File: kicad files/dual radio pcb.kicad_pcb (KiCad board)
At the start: 4 copper layers, 37.7 x 37.7 mm, 65 parts, among them J1 Conn_Coaxial, J2 Conn_01x01_Female, J3 Conn_01x01_Female, J4 Conn_01x01_Female, J5 Conn_01x01_Female, J6 Conn_01x01_Female, J7 Conn_01x04_Male, J8 Conn_Coaxial, J9 Conn_01x01_Female, U1 3V3. 500mA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

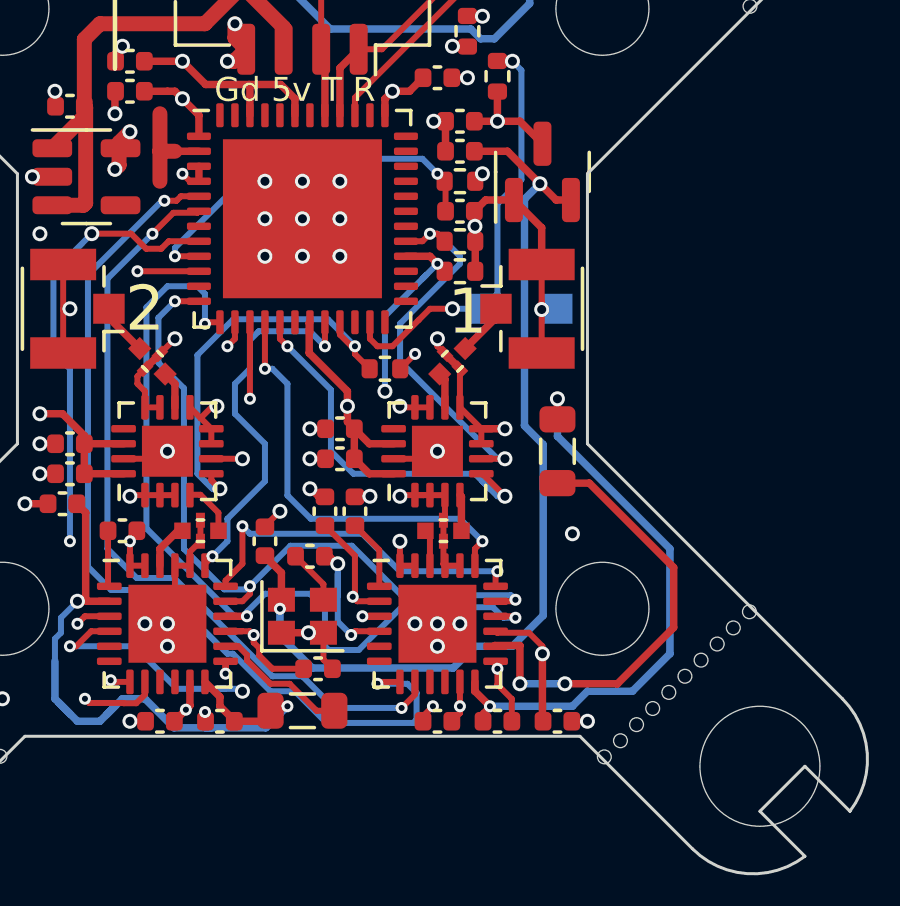
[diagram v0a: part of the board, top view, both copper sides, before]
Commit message: Updated dual radio to eliminate second rad's inductor
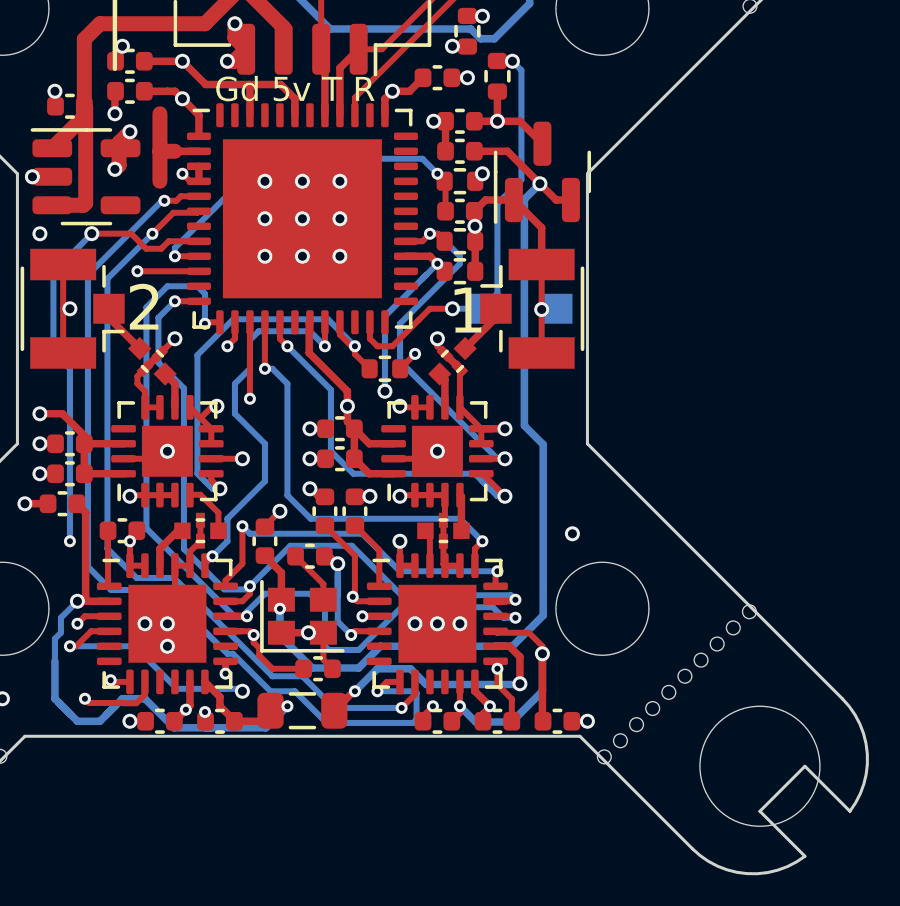
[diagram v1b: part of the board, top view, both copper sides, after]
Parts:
- removed L2: 15u, Inductor_SMD:L_0805_2012Metric
- moved L1 12.1 mm to (142.5, 120.9), turned to 0 degrees
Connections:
- C12 pad 1: /V_DCC_2 -> /V_DCC
- C13 pad 2: /V_DCC_2 -> /V_DCC
- U3 pad 12: /V_DCC_2 -> /V_DCC
- U3 pad 14: /V_DCC2_2 -> unconnected-(U3-Pad14)
- U3 pad 2: /V_DCC_2 -> /V_DCC
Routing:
- net /V_DCC_2: track 21.3 -> 0.00 mm, vias 2 -> 0
- net /V_DCC: track 29.2 -> 40.4 mm, vias 3 -> 4
- net /V_DCC2: track 15.1 -> 8.85 mm
- net +3V3: track 43.6 -> 48.2 mm
- net /V_DCC2_2: track 4.62 -> 0.00 mm
- net GND: vias 60 -> 59

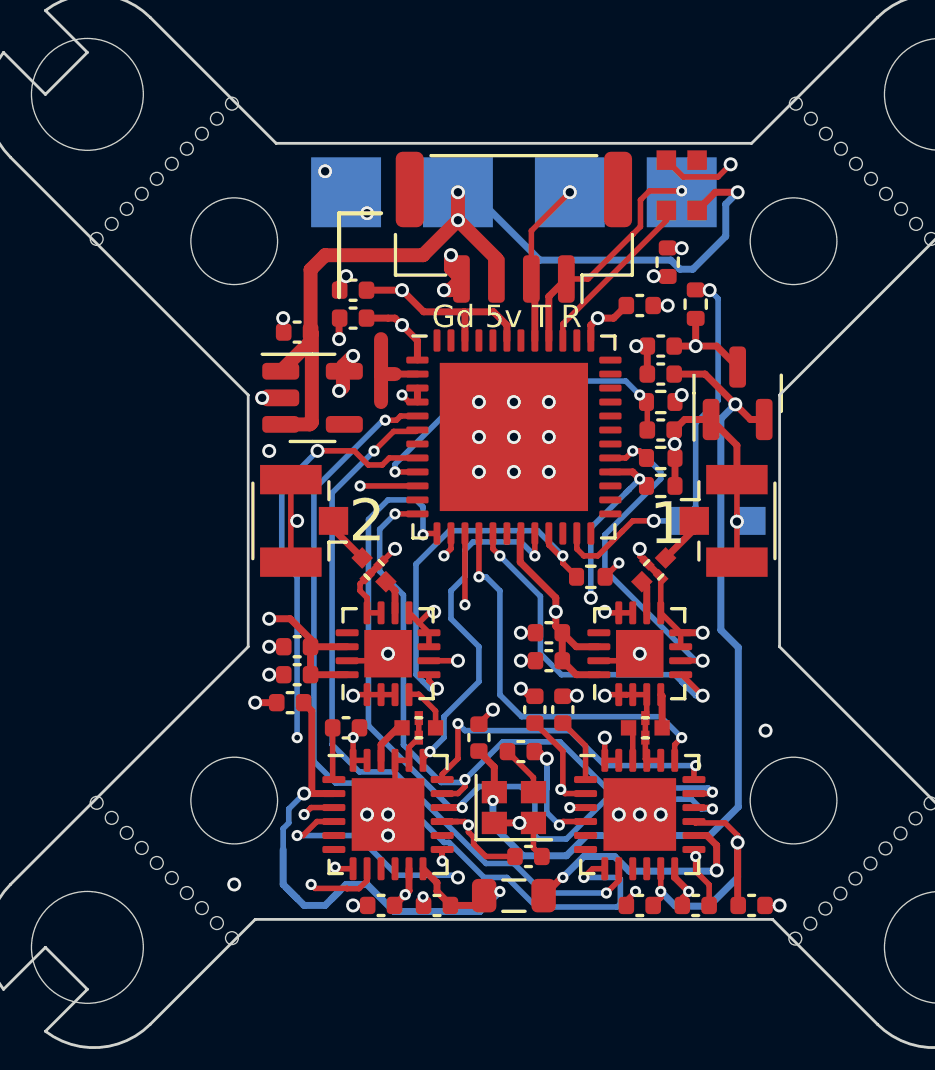
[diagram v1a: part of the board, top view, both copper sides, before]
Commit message: Updates including dif filter by antenna, better WiFi PCB antenna, and single inductor
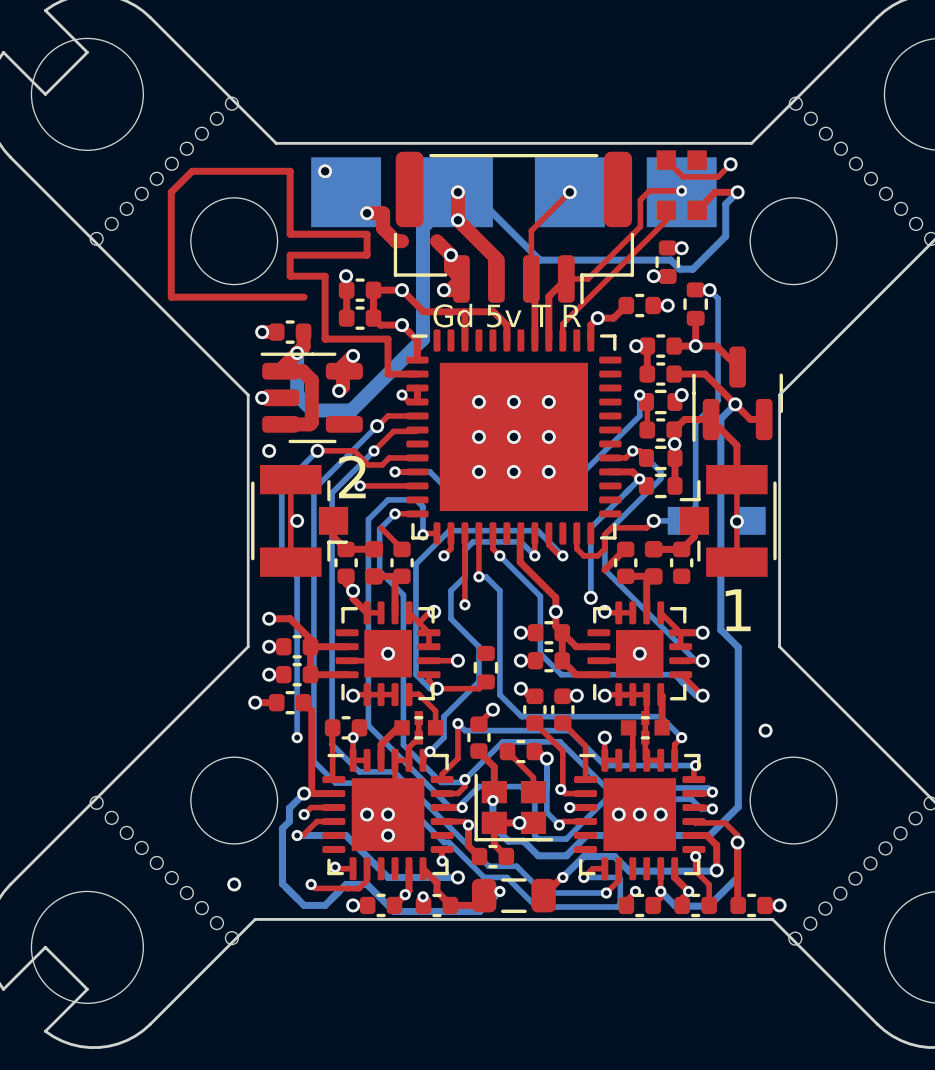
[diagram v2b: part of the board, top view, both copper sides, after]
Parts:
- removed U4, U5: 2450FM07D0034T, Anyleaf Shared:2450FM07D0034
- added C19: 1.2p, Capacitor_SMD:C_0402_1005Metric, F.Cu at (146.5, 109.0)
- added C22: 1.2p, Capacitor_SMD:C_0402_1005Metric, F.Cu at (138.5, 109.0)
- added C26: 1.2p, Capacitor_SMD:C_0402_1005Metric, F.Cu at (148.5, 109.0)
- added C27: 1.2p, Capacitor_SMD:C_0402_1005Metric, F.Cu at (136.5, 109.0)
- added L2: 3n, Inductor_SMD:L_0402_1005Metric, F.Cu at (147.5, 109.0)
- added L3: 3n, Inductor_SMD:L_0402_1005Metric, F.Cu at (137.5, 109.0)
- moved R4 4.96 mm to (141.5, 112.8), turned to 90 degrees
- moved C15 1.27 mm to (141.8, 119.5)
- moved C1 0.25 mm to (134.5, 100.8)
- moved C2 0.25 mm to (137.0, 100.2)
- moved C9 0.25 mm to (137.0, 99.2)
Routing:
- net /ANT_TRACE: track 3.55 -> 30.4 mm
- net /PWR_IN: track 33.1 -> 37.3 mm, vias 3 -> 4
- net GND: track 68.8 -> 71.6 mm, vias 59 -> 56
- net /ANT1: track 1.19 -> 2.32 mm
- net /ANT2: track 1.25 -> 2.31 mm
- net /PWR_TXEN2: track 13.7 -> 14.6 mm
- net +3V3: track 48.2 -> 47.6 mm

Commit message: Updated dual rad to use RFX2401C frontends
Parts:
- removed U12: AT2401C, Package_DFN_QFN:QFN-16-1EP_3x3mm_P0.5mm_EP1.7x1.7mm
- added U4: RFX2401C, Package_DFN_QFN:QFN-16-1EP_3x3mm_P0.5mm_EP1.7x1.7mm, F.Cu at (138.0, 112.2)
- U10, U9: footprint Anyleaf Shared:2450FM07D0034 -> Anyleaf_Shared:2450FM07D0034
- U13: value AT2401C -> RFX2401C
